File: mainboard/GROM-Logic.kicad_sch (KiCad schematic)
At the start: 34 parts, among them J5 UNICORN PORT, Q1 TIS92, U15 74LS04, U20 74LS04, U23 TMC0430, U24 TMC0430, U25 TMC0430, U26 TXB0104D, U27 TXB0104D, U28 TXB0104D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

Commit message: PCB routed
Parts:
- J5: footprint (none) -> Connector_PinHeader_2.54mm:PinHeader_1x15_P2.54mm_Vertical
- Q1: footprint (none) -> Package_TO_SOT_THT:TO-92_HandSolder
- R22: footprint Resistor_THT:R_Axial_DIN0207_L6.3mm_D2.5mm_P7.62mm_Horizontal -> Resistor_THT:R_Array_SIP10
- U15, U20, U6: footprint Package_DIP:DIP-14_W7.62mm_LongPads -> Package_DIP:DIP-14_W7.62mm_Socket_LongPads
- U22: renamed from U23; footprint Package_DIP:DIP-16_W7.62mm_LongPads -> Package_DIP:DIP-16_W7.62mm_Socket_LongPads
- U23: renamed from U24; footprint Package_DIP:DIP-16_W7.62mm_LongPads -> Package_DIP:DIP-16_W7.62mm_Socket_LongPads
- U24: renamed from U25; footprint Package_DIP:DIP-16_W7.62mm_LongPads -> Package_DIP:DIP-16_W7.62mm_Socket_LongPads
- renumbered U26 to U25, U27 to U26, U28 to U27, U29 to U28
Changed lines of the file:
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@@
   (symbol (lib_id "TI-Customs:TMC0430") (at 45.72 54.61 0) (unit 1)
     (in_bom yes) (on_board yes)
-    (property "Reference" "U23" (id 0) (at 55.88 27.94 0)
+    (property "Reference" "U22" (id 0) (at 55.88 27.94 0)
       (effects (font (size 1.524 1.524)))
     )
@@
       (effects (font (size 1.524 1.524)))
     )
-    (property "Footprint" "Package_DIP:DIP-16_W7.62mm_LongPads" (id 2) (at 45.72 54.61 0)
+    (property "Footprint" "Package_DIP:DIP-16_W7.62mm_Socket_LongPads" (id 2) (at 45.72 54.61 0)
       (effects (font (size 1.524 1.524)) hide)
     )
@@
   (symbol (lib_id "TI-Customs:TMC0430") (at 91.44 54.61 0) (unit 1)
     (in_bom yes) (on_board yes)
-    (property "Reference" "U24" (id 0) (at 101.6 27.94 0)
+    (property "Reference" "U23" (id 0) (at 101.6 27.94 0)
       (effects (font (size 1.524 1.524)))
     )
@@
       (effects (font (size 1.524 1.524)))
     )
-    (property "Footprint" "Package_DIP:DIP-16_W7.62mm_LongPads" (id 2) (at 91.44 54.61 0)
+    (property "Footprint" "Package_DIP:DIP-16_W7.62mm_Socket_LongPads" (id 2) (at 91.44 54.61 0)
       (effects (font (size 1.524 1.524)) hide)
     )
@@
   (symbol (lib_id "TI-Customs:TMC0430") (at 137.16 54.61 0) (unit 1)
     (in_bom yes) (on_board yes)
-    (property "Reference" "U25" (id 0) (at 147.32 27.94 0)
+    (property "Reference" "U24" (id 0) (at 147.32 27.94 0)
       (effects (font (size 1.524 1.524)))
     )
@@
       (effects (font (size 1.524 1.524)))
     )
-    (property "Footprint" "Package_DIP:DIP-16_W7.62mm_LongPads" (id 2) (at 137.16 54.61 0)
+    (property "Footprint" "Package_DIP:DIP-16_W7.62mm_Socket_LongPads" (id 2) (at 137.16 54.61 0)
       (effects (font (size 1.524 1.524)) hide)
     )
@@
       (effects (font (size 1.524 1.524)))
     )
-    (property "Footprint" "Package_DIP:DIP-14_W7.62mm_LongPads" (id 2) (at 41.91 124.46 0)
+    (property "Footprint" "Package_DIP:DIP-14_W7.62mm_Socket_LongPads" (id 2) (at 41.91 124.46 0)
       (effects (font (size 1.524 1.524)) hide)
     )
@@
       (effects (font (size 0.762 0.762)) (justify right))
     )
-    (property "Footprint" "Resistor_THT:R_Axial_DIN0207_L6.3mm_D2.5mm_P7.62mm_Horizontal" (id 2) (at 31.75 176.53 0)
+    (property "Footprint" "Resistor_THT:R_Array_SIP10" (id 2) (at 31.75 176.53 0)
       (effects (font (size 1.524 1.524)) hide)
     )
@@
       (effects (font (size 1.27 1.27)) (justify left))
     )
-    (property "Footprint" "" (id 2) (at 44.45 184.785 0)
+    (property "Footprint" "Package_TO_SOT_THT:TO-92_HandSolder" (id 2) (at 44.45 184.785 0)
       (effects (font (size 1.27 1.27) italic) (justify left) hide)
     )
@@
       (effects (font (size 1.524 1.524)))
     )
-    (property "Footprint" "Package_DIP:DIP-14_W7.62mm_LongPads" (id 2) (at 69.85 182.88 0)
+    (property "Footprint" "Package_DIP:DIP-14_W7.62mm_Socket_LongPads" (id 2) (at 69.85 182.88 0)
       (effects (font (size 1.524 1.524)) hide)
     )
@@
       (effects (font (size 1.524 1.524)))
     )
-    (property "Footprint" "Package_DIP:DIP-14_W7.62mm_LongPads" (id 2) (at 43.18 137.16 0)
+    (property "Footprint" "Package_DIP:DIP-14_W7.62mm_Socket_LongPads" (id 2) (at 43.18 137.16 0)
       (effects (font (size 1.524 1.524)) hide)
     )
@@
       (effects (font (size 1.524 1.524)))
     )
-    (property "Footprint" "Package_DIP:DIP-14_W7.62mm_LongPads" (id 2) (at 58.42 134.62 0)
+    (property "Footprint" "Package_DIP:DIP-14_W7.62mm_Socket_LongPads" (id 2) (at 58.42 134.62 0)
       (effects (font (size 1.524 1.524)) hide)
     )
@@
   (symbol (lib_id "Logic_LevelTranslator:TXB0104D") (at 195.58 57.15 0) (unit 1)
     (in_bom yes) (on_board yes) (fields_autoplaced)
-    (property "Reference" "U26" (id 0) (at 197.5994 74.93 0)
+    (property "Reference" "U25" (id 0) (at 197.5994 74.93 0)
       (effects (font (size 1.27 1.27)) (justify left))
     )
@@
       (effects (font (size 1.27 1.27)) (justify right))
     )
-    (property "Footprint" "" (id 2) (at 165.1 111.76 0)
+    (property "Footprint" "Connector_PinHeader_2.54mm:PinHeader_1x15_P2.54mm_Vertical" (id 2) (at 165.1 111.76 0)
       (effects (font (size 1.27 1.27)) hide)
     )
@@
   (symbol (lib_id "Logic_LevelTranslator:TXB0104D") (at 252.73 116.84 0) (unit 1)
     (in_bom yes) (on_board yes) (fields_autoplaced)
-    (property "Reference" "U29" (id 0) (at 254.7494 134.62 0)
+    (property "Reference" "U28" (id 0) (at 254.7494 134.62 0)
       (effects (font (size 1.27 1.27)) (justify left))
     )
@@
   (symbol (lib_id "Logic_LevelTranslator:TXB0104D") (at 196.85 116.84 0) (unit 1)
     (in_bom yes) (on_board yes) (fields_autoplaced)
-    (property "Reference" "U27" (id 0) (at 198.8694 134.62 0)
+    (property "Reference" "U26" (id 0) (at 198.8694 134.62 0)
       (effects (font (size 1.27 1.27)) (justify left))
     )
@@
   (symbol (lib_id "Logic_LevelTranslator:TXB0104D") (at 250.19 55.88 0) (unit 1)
     (in_bom yes) (on_board yes) (fields_autoplaced)
-    (property "Reference" "U28" (id 0) (at 252.2094 73.66 0)
-      (effects (font (size 1.27 1.27)) (justify left))
-    )
+    (property "Reference" "U27" (id 0) (at 252.2094 73.66 0)
+      (effects (font (size 1.27 1.27)) (justify left))
+    )

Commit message: unicorn work
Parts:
- removed A1: Adafruit_Feather_HUZZAH32_ESP32, Module:Adafruit_Feather, symbol MCU_Module:Adafruit_Feather_HUZZAH32_ESP32
- removed C44, C45, C46, C47, C48, C49, C50, C51: .01µF, Capacitor_THT:C_Rect_L7.0mm_W2.0mm_P5.00mm, symbol Device:C
- removed R28, R29, R30, R31: 10KΩ, Resistor_THT:R_Axial_DIN0207_L6.3mm_D2.5mm_P7.62mm_Horizontal, symbol Device:R
- removed U25, U26, U27, U28: TXB0104D, Package_SO:SOIC-14_3.9x8.7mm_P1.27mm, symbol Logic_LevelTranslator:TXB0104D
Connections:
- net LV_A14 is gone; now on net IO_A14: J5.11 (Pin_11)
- net LV_D0 is gone; now on net D0: J5.1 (Pin_1)
- net LV_D1 is gone; now on net D1: J5.2 (Pin_2)
- net LV_D2 is gone; now on net D2: J5.3 (Pin_3)
- net LV_D3 is gone; now on net D3: J5.4 (Pin_4)
- net LV_D4 is gone; now on net D4: J5.5 (Pin_5)
- net LV_D5 is gone; now on net D5: J5.6 (Pin_6)
- net LV_D6 is gone; now on net D6: J5.7 (Pin_7)
- net LV_D7 is gone; now on net D7: J5.8 (Pin_8)
- net LV_DBIN is gone; now on net DBIN: J5.10 (Pin_10)
- net LV_GREADY is gone; now on net GREADY: J5.9 (Pin_9)
- net LV_GRMCLK is gone; now on net GRMCLK: J5.12 (Pin_12)
- net ~{LV_GS} is gone; now on net ~{GS}: J5.13 (Pin_13)
- no-connect marks 18 -> 1
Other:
- note added: "GROMs are left in for compatibility, in case GROM chips are available for testing. The intention is to emulate the GROMS with an ESP32 via the Unicorn port."
- note removed: "GROMs are left in for compatibility, in case GROM chips are available for testing. The intention is to emulate the GROMS with an ESP32."
- moved on the sheet: J5

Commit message: unicorn work
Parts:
- removed J5: UNICORN PORT, Connector_PinHeader_2.54mm:PinHeader_1x15_P2.54mm_Vertical, symbol Connector:Conn_01x15_Male
- added J5: UNICORN PORT, Connector_PinHeader_2.54mm:PinHeader_1x16_P2.54mm_Vertical, symbol Connector:Conn_01x16_Male
- renumbered C43 to C51
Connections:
- net +5V: now also J5.14 (Pin_14)
- net D0: now also J5.1 (Pin_1)
- net D1: now also J5.2 (Pin_2)
- net D2: now also J5.3 (Pin_3)
- net D3: now also J5.4 (Pin_4)
- net D4: now also J5.5 (Pin_5)
- net D5: now also J5.6 (Pin_6)
- net D6: now also J5.7 (Pin_7)
- net D7: now also J5.8 (Pin_8)
- net DBIN: now also J5.10 (Pin_10)
- net GND: now also J5.15 (Pin_15)
- net GREADY: now also J5.9 (Pin_9)
- net GRMCLK: now also J5.12 (Pin_12)
- net IO_A14: now also J5.11 (Pin_11)
- net ~{GS}: now also J5.13 (Pin_13)
- new net ~{RESET}: J5.16 (Pin_16)
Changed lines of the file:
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@@
+    (stroke (width 0) (type default) (color 0 0 0 0))
+  )
+  (wire (pts (xy 124.46 171.45) (xy 127 171.45))
     (stroke (width 0) (type default) (color 0 0 0 0))
   )
@@
     (stroke (width 0) (type default) (color 0 0 0 0))
   )
-  (wire (pts (xy 121.92 168.91) (xy 127 168.91))
+  (wire (pts (xy 109.22 168.91) (xy 127 168.91))
     (stroke (width 0) (type default) (color 0 0 0 0))
   )
@@
     (effects (font (size 1.524 1.524)) (justify right))
     (property "Intersheet References" "${INTERSHEET_REFS}" (id 0) (at -163.83 46.99 0)
+      (effects (font (size 1.27 1.27)) hide)
+    )
+  )
+  (global_label "~{RESET}" (shape input) (at 124.46 171.45 180) (fields_autoplaced)
+    (effects (font (size 1.524 1.524)) (justify right))
+    (property "Intersheet References" "${INTERSHEET_REFS}" (id 0) (at 309.88 208.28 0)
       (effects (font (size 1.27 1.27)) hide)
     )
@@
   (symbol (lib_id "Console-rescue:+5V") (at 40.64 24.13 0) (unit 1)
     (in_bom yes) (on_board yes)
-    (property "Reference" "#PWR066" (id 0) (at 40.64 27.94 0)
+    (property "Reference" "#PWR067" (id 0) (at 40.64 27.94 0)
       (effects (font (size 1.27 1.27)) hide)
     )
@@
   (symbol (lib_id "Console-rescue:+5V") (at 86.36 24.13 0) (unit 1)
     (in_bom yes) (on_board yes)
-    (property "Reference" "#PWR074" (id 0) (at 86.36 27.94 0)
+    (property "Reference" "#PWR075" (id 0) (at 86.36 27.94 0)
       (effects (font (size 1.27 1.27)) hide)
     )
@@
   (symbol (lib_id "Console-rescue:+5V") (at 132.08 24.13 0) (unit 1)
     (in_bom yes) (on_board yes)
-    (property "Reference" "#PWR079" (id 0) (at 132.08 27.94 0)
+    (property "Reference" "#PWR080" (id 0) (at 132.08 27.94 0)
       (effects (font (size 1.27 1.27)) hide)
     )
@@
   (symbol (lib_id "Console-rescue:-5V") (at 40.64 85.09 180) (unit 1)
     (in_bom yes) (on_board yes)
-    (property "Reference" "#PWR067" (id 0) (at 40.64 87.63 0)
+    (property "Reference" "#PWR068" (id 0) (at 40.64 87.63 0)
       (effects (font (size 1.27 1.27)) hide)
     )
@@
   (symbol (lib_id "Console-rescue:-5V") (at 86.36 85.09 180) (unit 1)
     (in_bom yes) (on_board yes)
-    (property "Reference" "#PWR075" (id 0) (at 86.36 87.63 0)
+    (property "Reference" "#PWR076" (id 0) (at 86.36 87.63 0)
       (effects (font (size 1.27 1.27)) hide)
     )
@@
   (symbol (lib_id "Console-rescue:-5V") (at 132.08 85.09 180) (unit 1)
     (in_bom yes) (on_board yes)
-    (property "Reference" "#PWR080" (id 0) (at 132.08 87.63 0)
+    (property "Reference" "#PWR081" (id 0) (at 132.08 87.63 0)
       (effects (font (size 1.27 1.27)) hide)
     )
@@
   (symbol (lib_id "TI-Customs:C_Small") (at 43.18 24.13 90) (unit 1)
     (in_bom yes) (on_board yes)
-    (property "Reference" "C43" (id 0) (at 46.99 26.67 90)
+    (property "Reference" "C51" (id 0) (at 46.99 26.67 90)
       (effects (font (size 1.27 1.27)) (justify left))
     )
@@
   (symbol (lib_id "Console-rescue:GND") (at 45.72 24.13 90) (unit 1)
     (in_bom yes) (on_board yes)
-    (property "Reference" "#PWR068" (id 0) (at 52.07 24.13 0)
+    (property "Reference" "#PWR069" (id 0) (at 52.07 24.13 0)
       (effects (font (size 1.27 1.27)) hide)
     )
@@
   (symbol (lib_id "Console-rescue:+5V") (at 68.58 124.46 0) (unit 1)
     (in_bom yes) (on_board yes)
-    (property "Reference" "#PWR073" (id 0) (at 68.58 128.27 0)
+    (property "Reference" "#PWR074" (id 0) (at 68.58 128.27 0)
       (effects (font (size 1.27 1.27)) hide)
     )
@@
   (symbol (lib_id "Console-rescue:+12V") (at 46.99 158.75 0) (unit 1)
     (in_bom yes) (on_board yes)
-    (property "Reference" "#PWR069" (id 0) (at 46.99 162.56 0)
+    (property "Reference" "#PWR070" (id 0) (at 46.99 162.56 0)
       (effects (font (size 1.27 1.27)) hide)
     )
@@
   (symbol (lib_id "Console-rescue:GND") (at 46.99 190.5 0) (unit 1)
     (in_bom yes) (on_board yes)
-    (property "Reference" "#PWR070" (id 0) (at 46.99 196.85 0)
+    (property "Reference" "#PWR071" (id 0) (at 46.99 196.85 0)
       (effects (font (size 1.27 1.27)) hide)
     )
@@
   (symbol (lib_id "Console-rescue:GND") (at 60.96 173.99 270) (unit 1)
     (in_bom yes) (on_board yes)
-    (property "Reference" "#PWR072" (id 0) (at 54.61 173.99 0)
+    (property "Reference" "#PWR073" (id 0) (at 54.61 173.99 0)
       (effects (font (size 1.27 1.27)) hide)
     )
@@
   (symbol (lib_id "Console-rescue:+5V") (at 60.96 149.86 0) (unit 1)
     (in_bom yes) (on_board yes)
-    (property "Reference" "#PWR071" (id 0) (at 60.96 153.67 0)
+    (property "Reference" "#PWR072" (id 0) (at 60.96 153.67 0)
       (effects (font (size 1.27 1.27)) hide)
     )
@@
   (symbol (lib_id "Console-rescue:+5V") (at 114.3 166.37 90) (unit 1)
     (in_bom yes) (on_board yes)
-    (property "Reference" "#PWR077" (id 0) (at 118.11 166.37 0)
+    (property "Reference" "#PWR079" (id 0) (at 118.11 166.37 0)
       (effects (font (size 1.27 1.27)) hide)
     )
@@
     (pin "1")
   )
-  (symbol (lib_id "Connector:Conn_01x15_Male") (at 132.08 151.13 0) (mirror y) (unit 1)
-    (in_bom yes) (on_board yes)
-    (property "Reference" "J5" (id 0) (at 133.35 149.8599 0)
+  (symbol (lib_id "Connector:Conn_01x16_Male") (at 132.08 151.13 0) (mirror y) (unit 1)
+    (in_bom yes) (on_board yes)
+    (property "Reference" "J5" (id 0) (at 132.7912 151.5653 0)
       (effects (font (size 1.27 1.27)) (justify right))
     )
-    (property "Value" "UNICORN PORT" (id 1) (at 116.84 129.54 0)
+    (property "Value" "UNICORN PORT" (id 1) (at 127 129.54 0)
       (effects (font (size 1.27 1.27)) (justify right))
     )
-    (property "Footprint" "Connector_PinHeader_2.54mm:PinHeader_1x15_P2.54mm_Vertical" (id 2) (at 132.08 151.13 0)
+    (property "Footprint" "Connector_PinHeader_2.54mm:PinHeader_1x16_P2.54mm_Vertical" (id 2) (at 132.08 151.13 0)
       (effects (font (size 1.27 1.27)) hide)
     )
@@
     (pin "14")
     (pin "15")
+    (pin "16")
     (pin "2")
     (pin "3")
@@
     (pin "9")
   )
-  (symbol (lib_id "Console-rescue:GND") (at 121.92 168.91 0) (unit 1)
-    (in_bom yes) (on_board yes)
-    (property "Reference" "#PWR078" (id 0) (at 121.92 175.26 0)
-      (effects (font (size 1.27 1.27)) hide)
-    )
-    (property "Value" "GND" (id 1) (at 121.92 172.72 0))
-    (property "Footprint" "" (id 2) (at 121.92 168.91 0)
-      (effects (font (size 1.524 1.524)))
-    )
-    (property "Datasheet" "" (id 3) (at 121.92 168.91 0)
+  (symbol (lib_id "Console-rescue:GND") (at 109.22 168.91 0) (unit 1)
+    (in_bom yes) (on_board yes)
+    (property "Reference" "#PWR078" (id 0) (at 109.22 175.26 0)
+      (effects (font (size 1.27 1.27)) hide)
+    )
+    (property "Value" "GND" (id 1) (at 109.22 172.72 0))
+    (property "Footprint" "" (id 2) (at 109.22 168.91 0)
+      (effects (font (size 1.524 1.524)))
+    )
+    (property "Datasheet" "" (id 3) (at 109.22 168.91 0)
       (effects (font (size 1.524 1.524)))
     )
@@
   (symbol (lib_id "power:VSS") (at 97.79 92.71 0) (unit 1)
     (in_bom yes) (on_board yes)
-    (property "Reference" "#PWR076" (id 0) (at 97.79 96.52 0)
-      (effects (font (size 1.27 1.27)) hide)
-    )
+    (property "Reference" "#PWR077" (id 0) (at 97.79 96.52 0)
+      (effects (font (size 1.27 1.27)) hide)
+    )

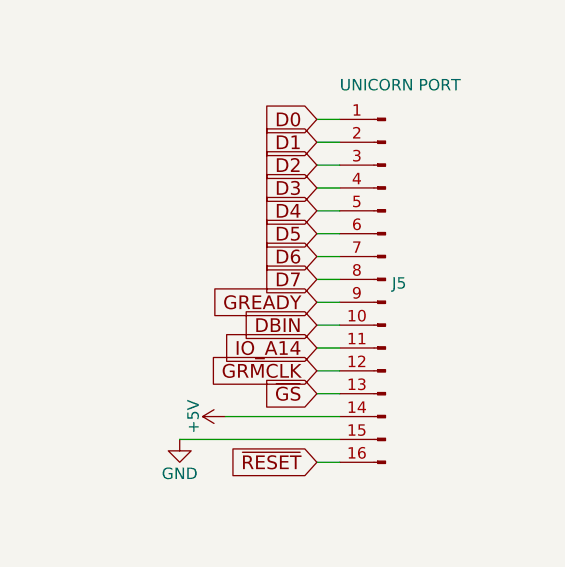
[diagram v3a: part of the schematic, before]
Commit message: Shrink PCB
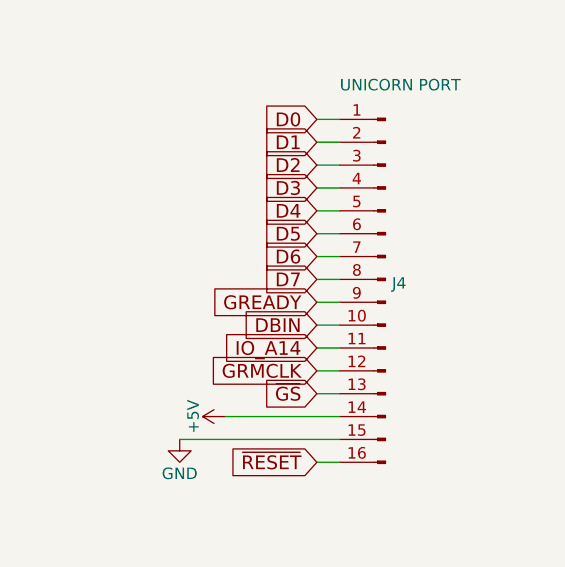
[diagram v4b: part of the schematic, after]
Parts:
- renumbered J5 to J4
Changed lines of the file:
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@@
   (symbol (lib_id "Connector:Conn_01x16_Male") (at 132.08 151.13 0) (mirror y) (unit 1)
     (in_bom yes) (on_board yes)
-    (property "Reference" "J5" (id 0) (at 132.7912 151.5653 0)
+    (property "Reference" "J4" (id 0) (at 132.7912 151.5653 0)
       (effects (font (size 1.27 1.27)) (justify right))
     )

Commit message: hardware updates
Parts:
- renumbered R22 to R21, R23 to R22, R24 to R23, R25 to R24, R26 to R25, R27 to R26
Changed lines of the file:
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@@
   (symbol (lib_id "Console-rescue:R") (at 68.58 128.27 0) (unit 1)
     (in_bom yes) (on_board yes)
-    (property "Reference" "R27" (id 0) (at 68.58 128.27 90))
+    (property "Reference" "R26" (id 0) (at 68.58 128.27 90))
     (property "Value" "4.7kΩ" (id 1) (at 66.04 128.27 90))
     (property "Footprint" "Resistor_THT:R_Axial_DIN0207_L6.3mm_D2.5mm_P7.62mm_Horizontal" (id 2) (at 66.802 128.27 90)
@@
   (symbol (lib_id "Device:R_Network09") (at 31.75 176.53 270) (unit 1)
     (in_bom yes) (on_board yes)
-    (property "Reference" "R22" (id 0) (at 30.48 189.23 90)
+    (property "Reference" "R21" (id 0) (at 30.48 189.23 90)
       (effects (font (size 0.762 0.762)) (justify left))
     )
@@
   (symbol (lib_id "Console-rescue:R_Small") (at 46.99 161.29 180) (unit 1)
     (in_bom yes) (on_board yes)
-    (property "Reference" "R23" (id 0) (at 48.26 161.29 90)
+    (property "Reference" "R22" (id 0) (at 48.26 161.29 90)
       (effects (font (size 1.27 1.27)) (justify bottom))
     )
@@
   (symbol (lib_id "Console-rescue:R_Small") (at 58.42 182.88 270) (unit 1)
     (in_bom yes) (on_board yes)
-    (property "Reference" "R24" (id 0) (at 58.42 181.61 90)
+    (property "Reference" "R23" (id 0) (at 58.42 181.61 90)
       (effects (font (size 1.27 1.27)) (justify bottom))
     )
@@
   (symbol (lib_id "Console-rescue:R_Small") (at 60.96 170.18 0) (unit 1)
     (in_bom yes) (on_board yes)
-    (property "Reference" "R26" (id 0) (at 61.722 169.672 0)
+    (property "Reference" "R25" (id 0) (at 61.722 169.672 0)
       (effects (font (size 1.27 1.27)) (justify left))
     )
@@
   (symbol (lib_id "Console-rescue:R_Small") (at 60.96 162.56 0) (unit 1)
     (in_bom yes) (on_board yes)
-    (property "Reference" "R25" (id 0) (at 61.722 162.052 0)
-      (effects (font (size 1.27 1.27)) (justify left))
-    )
+    (property "Reference" "R24" (id 0) (at 61.722 162.052 0)
+      (effects (font (size 1.27 1.27)) (justify left))
+    )

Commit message: PCB cleanup
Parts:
- removed U22, U23, U24: TMC0430, Package_DIP:DIP-16_W7.62mm_Socket_LongPads, symbol TI-Customs:TMC0430
- added U23, U24, U25: TMC0430, Package_DIP:DIP-16_W7.62mm_Socket_LongPads, symbol Werner_custom:TMC0430
- C51: symbol TI-Customs:C_Small -> Device:C
- CR2, CR3: symbol Console-rescue:D -> Device:D
- Q1: symbol Console-rescue:S8050 -> Device:Q_NPN_EBC
- R22, R23, R24, R25: symbol Console-rescue:R_Small -> Device:R_Small
- R26: symbol Console-rescue:R -> Device:R
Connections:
- net +5V: now also U23.9 (Vcc), U24.9 (Vcc), U25.9 (Vcc)
- net -5V: now also U23.14 (Vdd), U24.14 (Vdd), U25.14 (Vdd)
- net D0: now also U23.8 (D0_(MSB)), U24.8 (D0_(MSB)), U25.8 (D0_(MSB))
- net D1: now also U23.7 (D1), U24.7 (D1), U25.7 (D1)
- net D2: now also U23.6 (D2), U24.6 (D2), U25.6 (D2)
- net D3: now also U23.5 (D3), U24.5 (D3), U25.5 (D3)
- net D4: now also U23.4 (D4), U24.4 (D4), U25.4 (D4)
- net D5: now also U23.3 (D5), U24.3 (D5), U25.3 (D5)
- net D6: now also U23.2 (D6), U24.2 (D6), U25.2 (D6)
- net D7: now also U23.1 (D7_(LSB)), U24.1 (D7_(LSB)), U25.1 (D7_(LSB))
- net DBIN: now also U23.12 (M), U24.12 (M), U25.12 (M)
- net GREADY: now also U23.15 (GREADY), U24.15 (GREADY), U25.15 (GREADY)
- net GRMCLK: now also U23.13 (GRCLK), U24.13 (GRCLK), U25.13 (GRCLK)
- net IO_A14: now also U23.11 (MO), U24.11 (MO), U25.11 (MO)
- net VSS: now also U23.16 (Vss), U24.16 (Vss), U25.16 (Vss)
- net ~{GS}: now also U23.10 (~{GS}), U24.10 (~{GS}), U25.10 (~{GS})
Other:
- moved on the sheet: C51
